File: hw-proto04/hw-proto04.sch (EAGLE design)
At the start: 31 parts, among them IC1 VN5E160MSTR-E, IC2 UCC27523DR, IC3 MCP2562T, IC4 STM32F042C6T7, IC5 TLV74333PDBVR, J1 10, J2 10, Q1 SQJ147ELP-T1_GE3, Q2 SQJ147ELP-T1_GE3

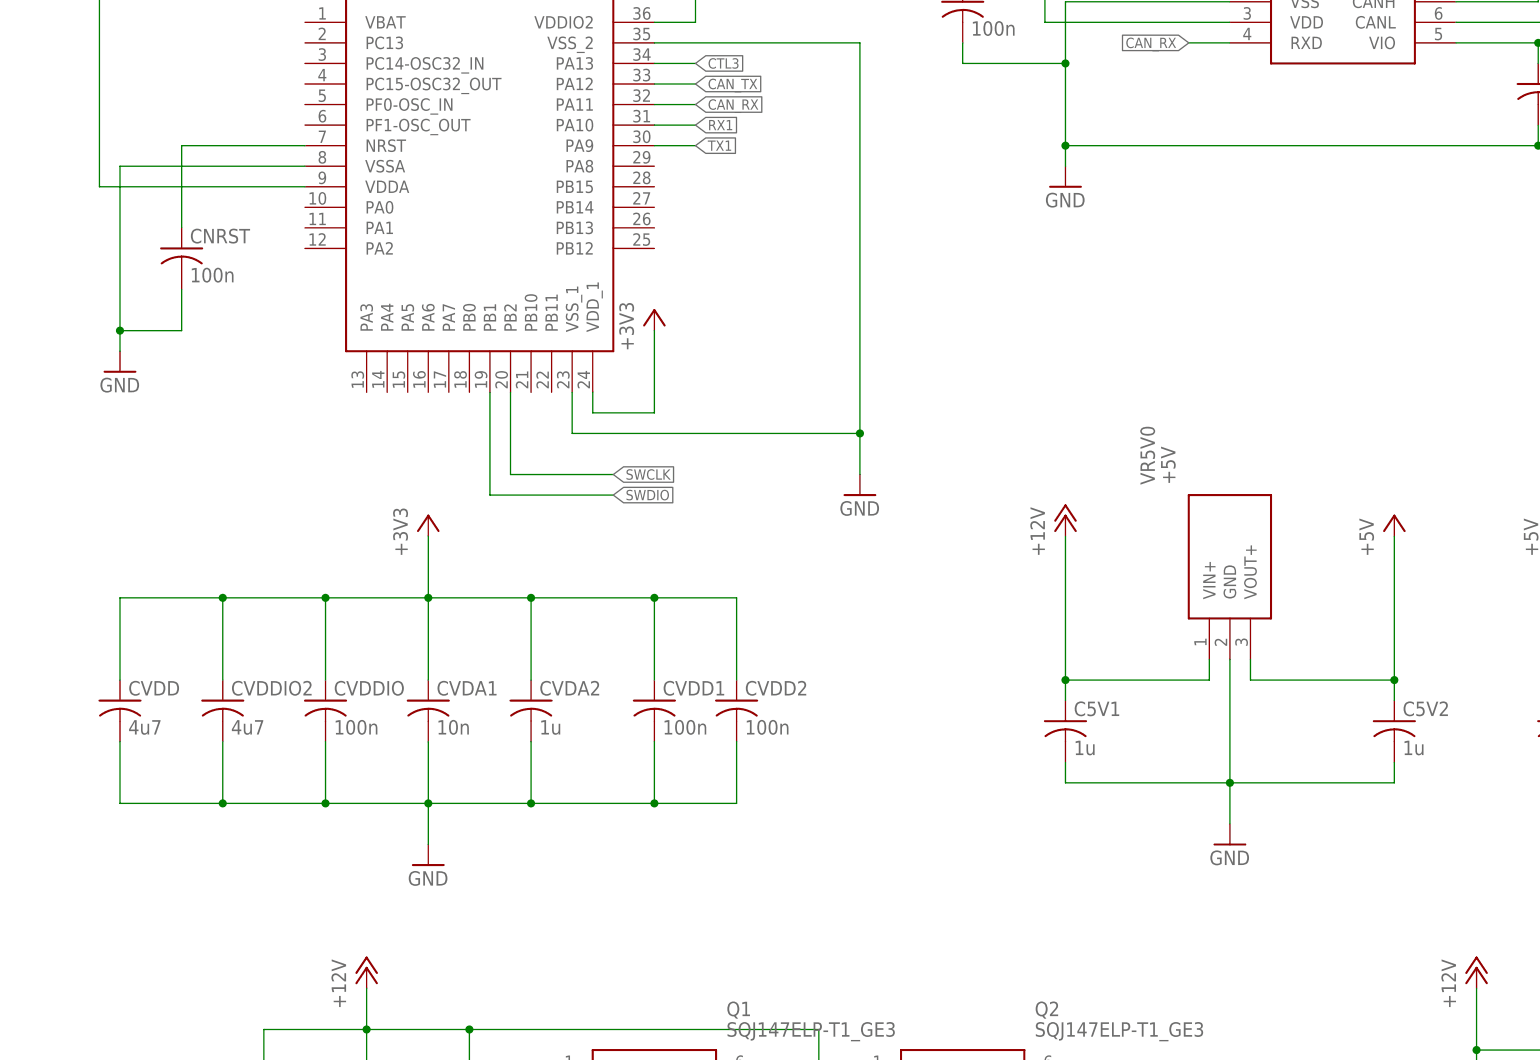
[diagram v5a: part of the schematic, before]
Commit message: added VBAT divider, refinements
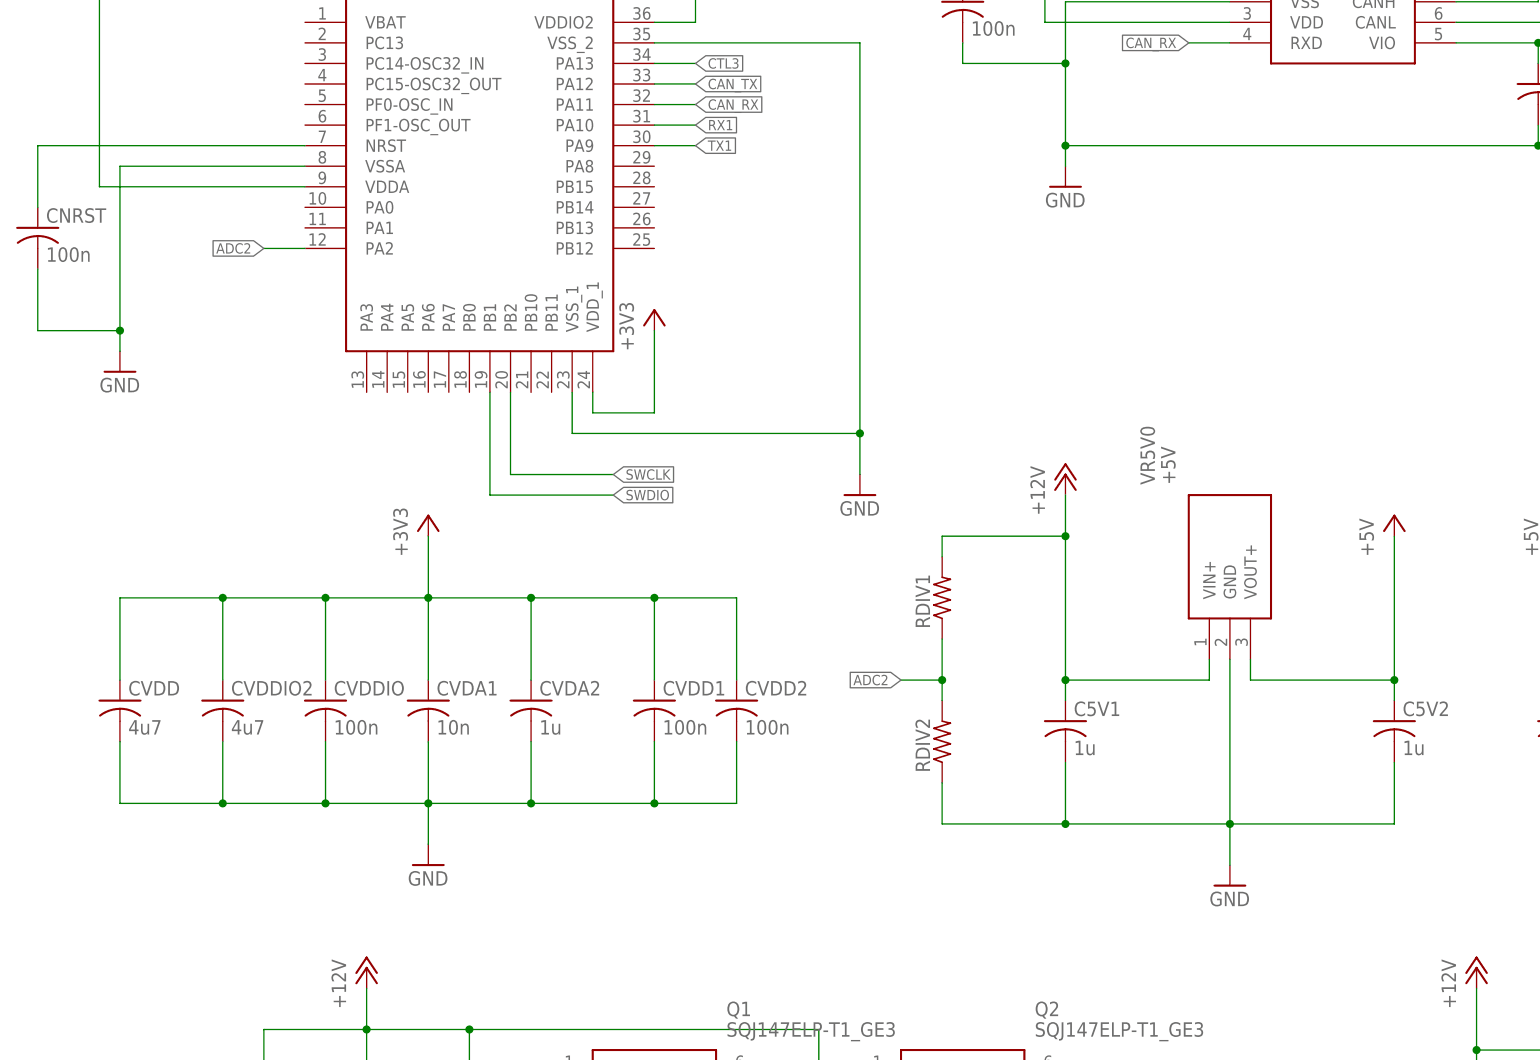
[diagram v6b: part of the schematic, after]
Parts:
- added RDIV1, RDIV2: (no value), rcl:R-US_R0805
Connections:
- net N$1 renamed CANH
- net N$2 renamed CANL
- new net ADC2: IC4.PA2, RDIV1.1, RDIV2.2
- net +12V: now also RDIV1.2
- net GND: now also RDIV2.1
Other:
- moved on the sheet: CNRST
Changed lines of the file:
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@@
 <part name="+3V8" library="supply1" deviceset="+3V3" device=""/>
 <part name="GND10" library="supply1" deviceset="GND" device=""/>
+<part name="RDIV1" library="rcl" deviceset="R-US_" device="R0805"/>
+<part name="RDIV2" library="rcl" deviceset="R-US_" device="R0805"/>
 </parts>
 <sheets>
@@
 <instance part="P+1" gate="1" x="-10.16" y="93.98"/>
 <instance part="P+2" gate="1" x="127" y="93.98"/>
-<instance part="P+4" gate="1" x="76.2" y="149.86"/>
+<instance part="P+4" gate="1" x="76.2" y="154.94"/>
 <instance part="VR5V0" gate="G$1" x="93.98" y="132.08" rot="R90"/>
-<instance part="GND8" gate="1" x="96.52" y="109.22"/>
+<instance part="GND8" gate="1" x="96.52" y="104.14"/>
 <instance part="P+5" gate="1" x="116.84" y="149.86"/>
 <instance part="+3V4" gate="G$1" x="142.24" y="231.14"/>
@@
 <instance part="Q2" gate="G$1" x="50.8" y="81.28"/>
 <instance part="CVDD2" gate="G$1" x="35.56" y="127"/>
-<instance part="CNRST" gate="G$1" x="-33.02" y="182.88"/>
+<instance part="CNRST" gate="G$1" x="-50.8" y="185.42"/>
 <instance part="IC2" gate="G$1" x="-27.94" y="50.8"/>
 <instance part="CDRV2" gate="G$1" x="-10.16" y="73.66"/>
@@
 <instance part="+3V8" gate="G$1" x="226.06" y="91.44"/>
 <instance part="GND10" gate="1" x="226.06" y="63.5"/>
+<instance part="RDIV1" gate="G$1" x="60.96" y="139.7" rot="R90"/>
+<instance part="RDIV2" gate="G$1" x="60.96" y="121.92" rot="R90"/>
 </instances>
 <busses>
@@
 <pinref part="VR5V0" gate="G$1" pin="GND"/>
 <pinref part="GND8" gate="1" pin="GND"/>
-<wire x1="96.52" y1="132.08" x2="96.52" y2="116.84" width="0.1524" layer="91"/>
+<wire x1="96.52" y1="132.08" x2="96.52" y2="111.76" width="0.1524" layer="91"/>
+<wire x1="96.52" y1="111.76" x2="96.52" y2="106.68" width="0.1524" layer="91"/>
+<pinref part="RDIV2" gate="G$1" pin="1"/>
+<wire x1="96.52" y1="111.76" x2="76.2" y2="111.76" width="0.1524" layer="91"/>
+<wire x1="76.2" y1="111.76" x2="60.96" y2="111.76" width="0.1524" layer="91"/>
+<wire x1="60.96" y1="111.76" x2="60.96" y2="116.84" width="0.1524" layer="91"/>
+<junction x="96.52" y="111.76"/>
+<pinref part="C5V2" gate="G$1" pin="2"/>
+<wire x1="96.52" y1="111.76" x2="116.84" y2="111.76" width="0.1524" layer="91"/>
+<wire x1="116.84" y1="111.76" x2="116.84" y2="119.38" width="0.1524" layer="91"/>
 <pinref part="C5V1" gate="G$1" pin="2"/>
-<wire x1="96.52" y1="116.84" x2="96.52" y2="111.76" width="0.1524" layer="91"/>
-<wire x1="96.52" y1="116.84" x2="76.2" y2="116.84" width="0.1524" layer="91"/>
-<wire x1="76.2" y1="116.84" x2="76.2" y2="119.38" width="0.1524" layer="91"/>
-<junction x="96.52" y="116.84"/>
-<pinref part="C5V2" gate="G$1" pin="2"/>
-<wire x1="96.52" y1="116.84" x2="116.84" y2="116.84" width="0.1524" layer="91"/>
-<wire x1="116.84" y1="116.84" x2="116.84" y2="119.38" width="0.1524" layer="91"/>
+<wire x1="76.2" y1="119.38" x2="76.2" y2="111.76" width="0.1524" layer="91"/>
+<junction x="76.2" y="111.76"/>
 </segment>
 <segment>
@@
 <pinref part="CNRST" gate="G$1" pin="2"/>
 <wire x1="-40.64" y1="172.72" x2="-40.64" y2="170.18" width="0.1524" layer="91"/>
-<wire x1="-33.02" y1="177.8" x2="-33.02" y2="172.72" width="0.1524" layer="91"/>
-<wire x1="-33.02" y1="172.72" x2="-40.64" y2="172.72" width="0.1524" layer="91"/>
+<wire x1="-50.8" y1="180.34" x2="-50.8" y2="172.72" width="0.1524" layer="91"/>
+<wire x1="-50.8" y1="172.72" x2="-40.64" y2="172.72" width="0.1524" layer="91"/>
 <junction x="-40.64" y="172.72"/>
 </segment>
@@
 </segment>
 </net>
-<net name="N$1" class="0">
+<net name="CANH" class="0">
 <segment>
 <pinref part="IC3" gate="G$1" pin="CANH"/>
@@
 </segment>
 </net>
-<net name="N$2" class="0">
+<net name="CANL" class="0">
 <segment>
 <pinref part="IC3" gate="G$1" pin="CANL"/>
@@
 <wire x1="76.2" y1="129.54" x2="76.2" y2="147.32" width="0.1524" layer="91"/>
 <pinref part="C5V1" gate="G$1" pin="1"/>
+<wire x1="76.2" y1="147.32" x2="76.2" y2="152.4" width="0.1524" layer="91"/>
 <wire x1="76.2" y1="127" x2="76.2" y2="129.54" width="0.1524" layer="91"/>
 <junction x="76.2" y="129.54"/>
+<pinref part="RDIV1" gate="G$1" pin="2"/>
+<wire x1="60.96" y1="144.78" x2="60.96" y2="147.32" width="0.1524" layer="91"/>
+<wire x1="60.96" y1="147.32" x2="76.2" y2="147.32" width="0.1524" layer="91"/>
+<junction x="76.2" y="147.32"/>
 </segment>
 <segment>
@@
 <pinref part="IC4" gate="G$1" pin="NRST"/>
 <pinref part="CNRST" gate="G$1" pin="1"/>
-<wire x1="-17.78" y1="195.58" x2="-33.02" y2="195.58" width="0.1524" layer="91"/>
-<wire x1="-33.02" y1="195.58" x2="-33.02" y2="185.42" width="0.1524" layer="91"/>
+<wire x1="-17.78" y1="195.58" x2="-50.8" y2="195.58" width="0.1524" layer="91"/>
+<wire x1="-50.8" y1="195.58" x2="-50.8" y2="187.96" width="0.1524" layer="91"/>
 </segment>
 </net>
@@
 </segment>
 </net>
+<net name="ADC2" class="0">
+<segment>
+<pinref part="IC4" gate="G$1" pin="PA2"/>
+<wire x1="-22.86" y1="182.88" x2="-17.78" y2="182.88" width="0.1524" layer="91"/>
+<label x="-22.86" y="182.88" size="1.27" layer="95" rot="R180" xref="yes"/>
+</segment>
+<segment>
+<pinref part="RDIV2" gate="G$1" pin="2"/>
+<pinref part="RDIV1" gate="G$1" pin="1"/>
+<wire x1="60.96" y1="127" x2="60.96" y2="129.54" width="0.1524" layer="91"/>
+<wire x1="60.96" y1="129.54" x2="60.96" y2="134.62" width="0.1524" layer="91"/>
+<wire x1="55.88" y1="129.54" x2="60.96" y2="129.54" width="0.1524" layer="91"/>
+<junction x="60.96" y="129.54"/>
+<label x="55.88" y="129.54" size="1.27" layer="95" rot="R180" xref="yes"/>
+</segment>
+</net>

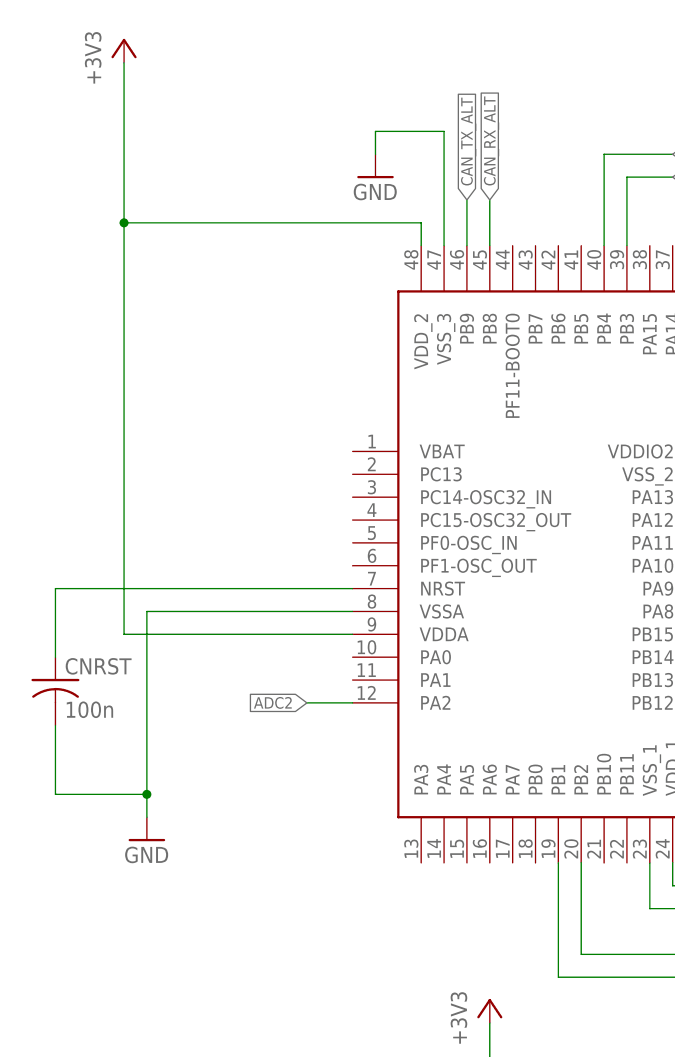
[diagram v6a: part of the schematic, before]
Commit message: added boot0 pulldown
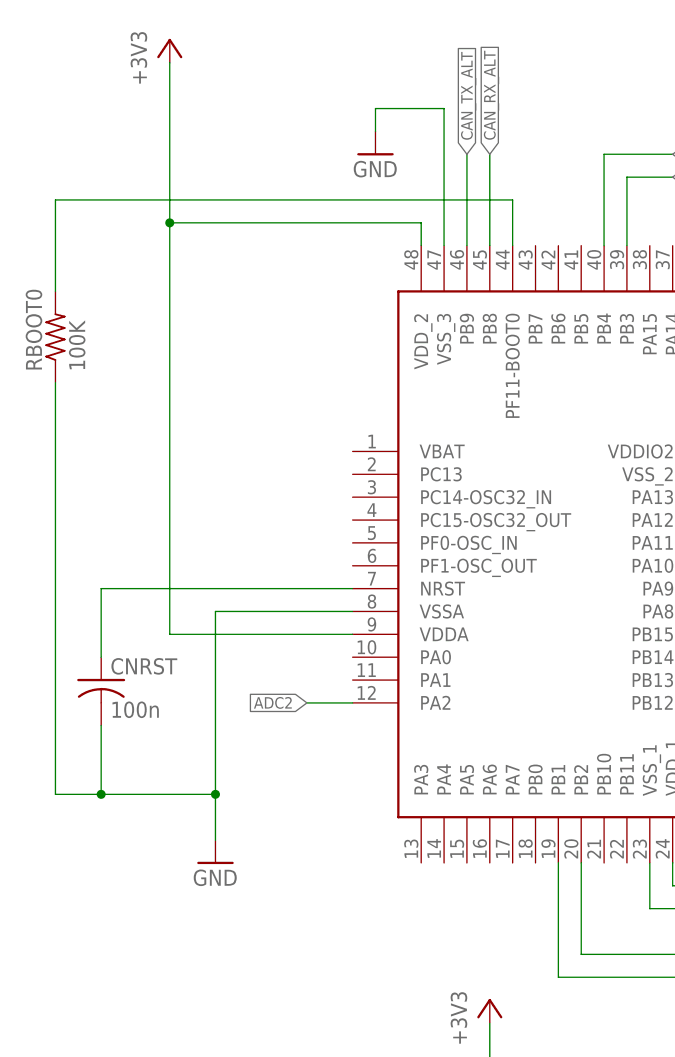
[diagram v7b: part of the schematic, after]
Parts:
- added RBOOT0: 100K, rcl:R-US_R0603
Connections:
- new net BOOT0: IC4.PF11-BOOT0, RBOOT0.2
- net GND: now also RBOOT0.1
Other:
- moved on the sheet: CNRST
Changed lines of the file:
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@@
 <part name="RDIV1" library="rcl" deviceset="R-US_" device="R0805"/>
 <part name="RDIV2" library="rcl" deviceset="R-US_" device="R0805"/>
+<part name="RBOOT0" library="rcl" deviceset="R-US_" device="R0603" value="100K"/>
 </parts>
 <sheets>
@@
 <instance part="GND7" gate="1" x="144.78" y="109.22"/>
 <instance part="+3V1" gate="G$1" x="185.42" y="149.86"/>
-<instance part="+3V2" gate="G$1" x="-43.18" y="256.54"/>
+<instance part="+3V2" gate="G$1" x="-38.1" y="256.54"/>
 <instance part="P+1" gate="1" x="-10.16" y="93.98"/>
 <instance part="P+2" gate="1" x="127" y="93.98"/>
@@
 <instance part="Q2" gate="G$1" x="50.8" y="81.28"/>
 <instance part="CVDD2" gate="G$1" x="35.56" y="127"/>
-<instance part="CNRST" gate="G$1" x="-50.8" y="185.42"/>
+<instance part="CNRST" gate="G$1" x="-45.72" y="185.42"/>
 <instance part="IC2" gate="G$1" x="-27.94" y="50.8"/>
 <instance part="CDRV2" gate="G$1" x="-10.16" y="73.66"/>
@@
 <instance part="+3V5" gate="G$1" x="25.4" y="175.26"/>
 <instance part="+3V6" gate="G$1" x="30.48" y="256.54"/>
-<instance part="GND12" gate="1" x="-15.24" y="241.3"/>
+<instance part="GND12" gate="1" x="-15.24" y="243.84"/>
 <instance part="IC5" gate="G$1" x="152.4" y="137.16"/>
 <instance part="P+3" gate="1" x="137.16" y="149.86"/>
@@
 <instance part="CVDDIO" gate="G$1" x="-15.24" y="127"/>
 <instance part="GND13" gate="1" x="-2.54" y="106.68"/>
-<instance part="GND5" gate="1" x="-40.64" y="167.64"/>
+<instance part="GND5" gate="1" x="-33.02" y="165.1"/>
 <instance part="+3V3" gate="G$1" x="182.88" y="91.44"/>
 <instance part="PRG" gate="G$1" x="203.2" y="78.74" rot="R180"/>
@@
 <instance part="RDIV1" gate="G$1" x="60.96" y="139.7" rot="R90"/>
 <instance part="RDIV2" gate="G$1" x="60.96" y="121.92" rot="R90"/>
+<instance part="RBOOT0" gate="G$1" x="-50.8" y="223.52" rot="R90"/>
 </instances>
 <busses>
@@
 <segment>
 <pinref part="IC4" gate="G$1" pin="VSS_3"/>
-<wire x1="-7.62" y1="233.68" x2="-7.62" y2="246.38" width="0.1524" layer="91"/>
-<wire x1="-7.62" y1="246.38" x2="-15.24" y2="246.38" width="0.1524" layer="91"/>
-<wire x1="-15.24" y1="246.38" x2="-15.24" y2="243.84" width="0.1524" layer="91"/>
+<wire x1="-7.62" y1="233.68" x2="-7.62" y2="248.92" width="0.1524" layer="91"/>
+<wire x1="-7.62" y1="248.92" x2="-15.24" y2="248.92" width="0.1524" layer="91"/>
+<wire x1="-15.24" y1="248.92" x2="-15.24" y2="246.38" width="0.1524" layer="91"/>
 <pinref part="GND12" gate="1" pin="GND"/>
 </segment>
@@
 <segment>
 <pinref part="IC4" gate="G$1" pin="VSSA"/>
-<wire x1="-17.78" y1="193.04" x2="-40.64" y2="193.04" width="0.1524" layer="91"/>
-<wire x1="-40.64" y1="193.04" x2="-40.64" y2="172.72" width="0.1524" layer="91"/>
+<wire x1="-17.78" y1="193.04" x2="-33.02" y2="193.04" width="0.1524" layer="91"/>
+<wire x1="-33.02" y1="193.04" x2="-33.02" y2="172.72" width="0.1524" layer="91"/>
 <pinref part="GND5" gate="1" pin="GND"/>
 <pinref part="CNRST" gate="G$1" pin="2"/>
-<wire x1="-40.64" y1="172.72" x2="-40.64" y2="170.18" width="0.1524" layer="91"/>
-<wire x1="-50.8" y1="180.34" x2="-50.8" y2="172.72" width="0.1524" layer="91"/>
-<wire x1="-50.8" y1="172.72" x2="-40.64" y2="172.72" width="0.1524" layer="91"/>
-<junction x="-40.64" y="172.72"/>
+<wire x1="-33.02" y1="172.72" x2="-33.02" y2="167.64" width="0.1524" layer="91"/>
+<wire x1="-45.72" y1="180.34" x2="-45.72" y2="172.72" width="0.1524" layer="91"/>
+<wire x1="-45.72" y1="172.72" x2="-33.02" y2="172.72" width="0.1524" layer="91"/>
+<junction x="-33.02" y="172.72"/>
+<pinref part="RBOOT0" gate="G$1" pin="1"/>
+<wire x1="-50.8" y1="218.44" x2="-50.8" y2="172.72" width="0.1524" layer="91"/>
+<wire x1="-50.8" y1="172.72" x2="-45.72" y2="172.72" width="0.1524" layer="91"/>
+<junction x="-45.72" y="172.72"/>
 </segment>
 <segment>
@@
 <pinref part="IC4" gate="G$1" pin="VDD_2"/>
 <wire x1="-10.16" y1="233.68" x2="-10.16" y2="236.22" width="0.1524" layer="91"/>
-<wire x1="-10.16" y1="236.22" x2="-43.18" y2="236.22" width="0.1524" layer="91"/>
-<junction x="-43.18" y="236.22"/>
-<wire x1="-43.18" y1="236.22" x2="-43.18" y2="254" width="0.1524" layer="91"/>
+<wire x1="-10.16" y1="236.22" x2="-38.1" y2="236.22" width="0.1524" layer="91"/>
+<junction x="-38.1" y="236.22"/>
+<wire x1="-38.1" y1="236.22" x2="-38.1" y2="254" width="0.1524" layer="91"/>
 <pinref part="IC4" gate="G$1" pin="VDDA"/>
-<wire x1="-17.78" y1="190.5" x2="-43.18" y2="190.5" width="0.1524" layer="91"/>
-<wire x1="-43.18" y1="190.5" x2="-43.18" y2="236.22" width="0.1524" layer="91"/>
+<wire x1="-17.78" y1="190.5" x2="-38.1" y2="190.5" width="0.1524" layer="91"/>
+<wire x1="-38.1" y1="190.5" x2="-38.1" y2="236.22" width="0.1524" layer="91"/>
 </segment>
 <segment>
@@
 <pinref part="IC4" gate="G$1" pin="NRST"/>
 <pinref part="CNRST" gate="G$1" pin="1"/>
-<wire x1="-17.78" y1="195.58" x2="-50.8" y2="195.58" width="0.1524" layer="91"/>
-<wire x1="-50.8" y1="195.58" x2="-50.8" y2="187.96" width="0.1524" layer="91"/>
+<wire x1="-17.78" y1="195.58" x2="-45.72" y2="195.58" width="0.1524" layer="91"/>
+<wire x1="-45.72" y1="195.58" x2="-45.72" y2="187.96" width="0.1524" layer="91"/>
 </segment>
 </net>
@@
 <segment>
 <pinref part="IC4" gate="G$1" pin="PB9"/>
-<wire x1="-5.08" y1="238.76" x2="-5.08" y2="233.68" width="0.1524" layer="91"/>
-<label x="-5.08" y="238.76" size="1.27" layer="95" rot="R90" xref="yes"/>
+<wire x1="-5.08" y1="243.84" x2="-5.08" y2="233.68" width="0.1524" layer="91"/>
+<label x="-5.08" y="243.84" size="1.27" layer="95" rot="R90" xref="yes"/>
 </segment>
 </net>
@@
 <segment>
 <pinref part="IC4" gate="G$1" pin="PB8"/>
-<wire x1="-2.54" y1="238.76" x2="-2.54" y2="233.68" width="0.1524" layer="91"/>
-<label x="-2.54" y="238.76" size="1.27" layer="95" rot="R90" xref="yes"/>
+<wire x1="-2.54" y1="243.84" x2="-2.54" y2="233.68" width="0.1524" layer="91"/>
+<label x="-2.54" y="243.84" size="1.27" layer="95" rot="R90" xref="yes"/>
 </segment>
 </net>
@@
 </segment>
 </net>
+<net name="BOOT0" class="0">
+<segment>
+<pinref part="IC4" gate="G$1" pin="PF11-BOOT0"/>
+<wire x1="0" y1="233.68" x2="0" y2="238.76" width="0.1524" layer="91"/>
+<pinref part="RBOOT0" gate="G$1" pin="2"/>
+<wire x1="0" y1="238.76" x2="-50.8" y2="238.76" width="0.1524" layer="91"/>
+<wire x1="-50.8" y1="238.76" x2="-50.8" y2="228.6" width="0.1524" layer="91"/>
+</segment>
+</net>
